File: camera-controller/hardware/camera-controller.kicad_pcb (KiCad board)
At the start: 4 copper layers, 76 parts, among them J1 USB_C_Receptacle_USB2.0_14P, J2 Conn_Coaxial, J3 Conn_01x04, J4 Conn_01x08, J5 Micro_SD_Card_Det1, J6 Conn_01x02, U1 STM32H523RCTx, U2 LR2021, U3 MIC5504-3.3YM5, Y1 32.768MHz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

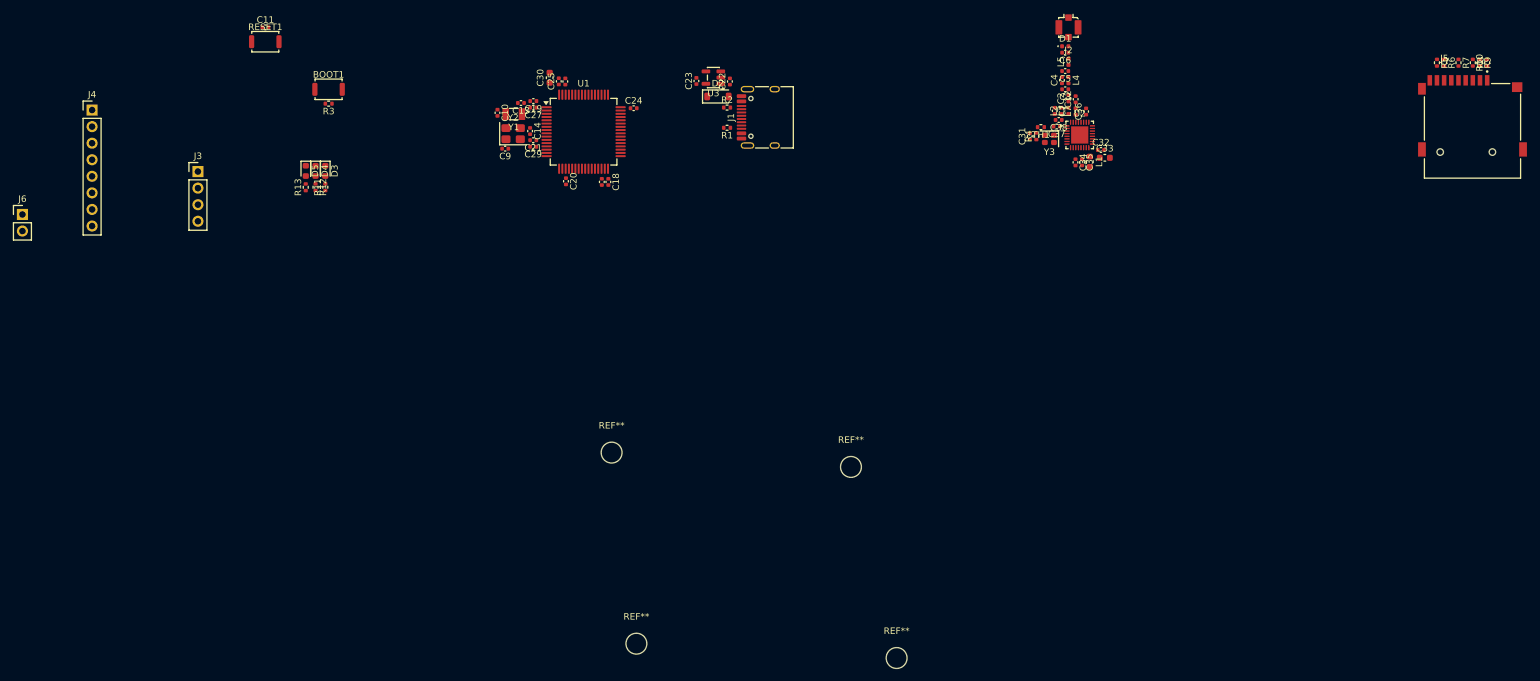
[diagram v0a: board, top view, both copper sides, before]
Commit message: made camera controller pcb layout
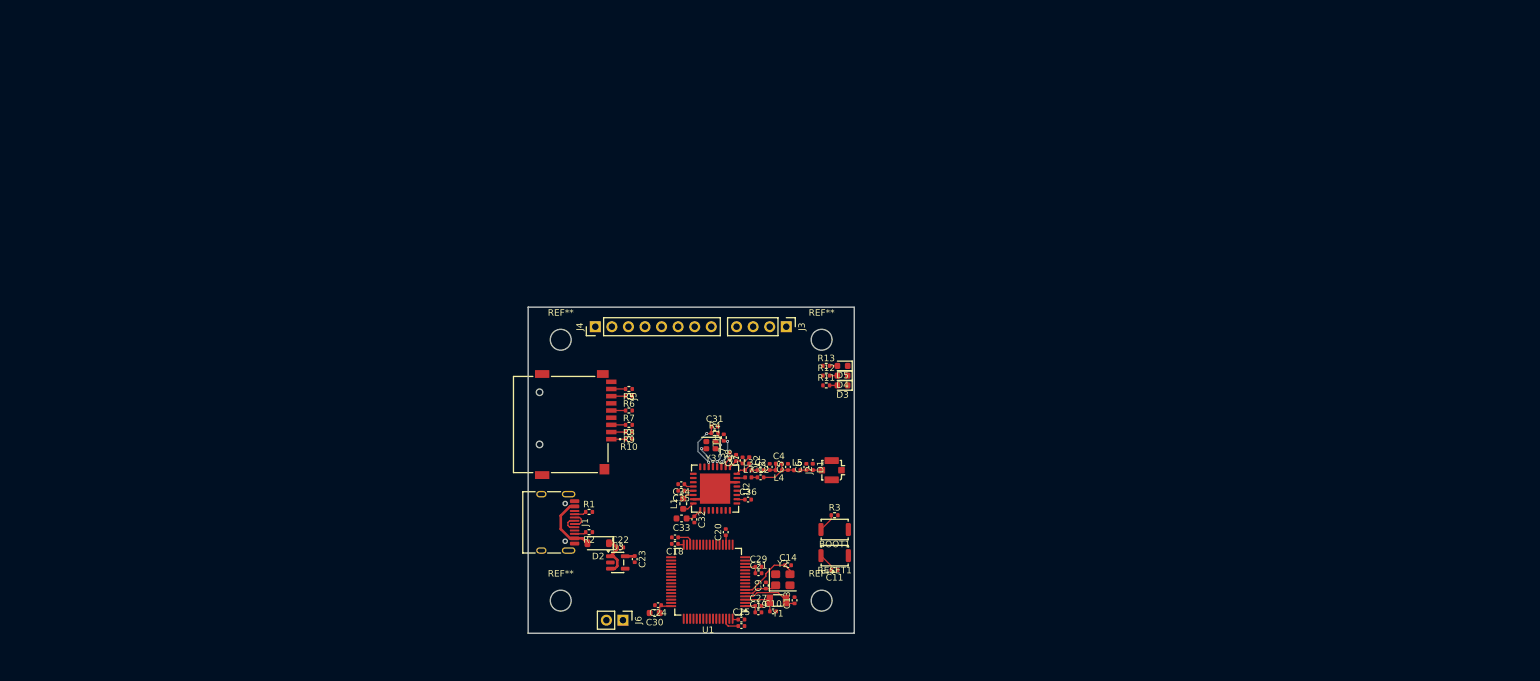
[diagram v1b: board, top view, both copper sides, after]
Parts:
- U2: footprint Package_DFN_QFN:QFN-32-1EP_4x4mm_P0.4mm_EP2.65x2.65mm -> Package_DFN_QFN:QFN-32-1EP_7x7mm_P0.65mm_EP4.65x4.65mm
- moved J5 146.9 mm to (110.0, 83.0), turned to -90 degrees
- moved R10 143.7 mm to (120.5, 85.2), turned to 180 degrees
- moved R9 142.3 mm to (120.5, 84.2), turned to 180 degrees
- moved R8 140.8 mm to (120.5, 83.0), turned to 180 degrees
- moved R7 137.9 mm to (120.5, 80.8), turned to 180 degrees
- moved R6 135.1 mm to (120.5, 78.7), turned to 180 degrees
- moved R5 133.6 mm to (120.5, 77.5), turned to 180 degrees
- moved C11 120.6 mm to (152.0, 105.3), turned to 180 degrees
- moved RESET1 117.6 mm to (152.0, 103.1), turned to 180 degrees
- moved J6 111.1 mm to (119.5, 113.0), turned to -90 degrees
- moved BOOT1 102.8 mm to (152.0, 99.1), turned to 180 degrees
- moved R3 100.0 mm to (152.0, 96.9), turned to 0 degrees
- moved J3 93.3 mm to (144.6, 68.0), turned to -90 degrees
- moved C26 87.8 mm to (137.7, 113.9), turned to 0 degrees
- moved D5 87.6 mm to (153.2, 74.0), turned to 180 degrees
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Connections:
- C7 pad 1: /VRPA -> /VR_PA
- L2 pad 1: /VRPA -> /VR_PA
- U1 pad 14: unconnected-(U1-PA0-Pad14) -> /CAM_STAT
- U1 pad 15: /CAM_STAT -> /LR_STAT
- U1 pad 16: /LR_STAT -> /LR_BUSY
- U1 pad 17: unconnected-(U1-PA3-Pad17) -> /LR_CS
- U1 pad 24: /LR_CS -> /LR_RST
- U1 pad 26: /LR_RST -> /LR_D5
- U1 pad 27: /LR_BUSY -> /LR_D6
- U1 pad 39: /LR_D6 -> unconnected-(U1-PC8-Pad39)
- U1 pad 41: /LR_D5 -> unconnected-(U1-PA8-Pad41)
- U1 pad 42: unconnected-(U1-PA9-Pad42) -> /UART_RX
- U1 pad 43: unconnected-(U1-PA10-Pad43) -> /UART_TX
- U1 pad 49: /SWCKL -> /SWCLK
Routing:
- net +3.3V: track 0.00 -> 15.4 mm
- net Net-(D2-A): track 0.00 -> 9.75 mm
- net /HSE_OUT: track 0.00 -> 9.59 mm
- net /LSE_OUT: track 0.00 -> 8.50 mm
- net /VNTC: track 0.00 -> 8.08 mm, vias 0 -> 2
- net GND: track 0.00 -> 7.75 mm
- net Net-(D2-K): track 0.00 -> 6.75 mm
- net /NTC: track 0.00 -> 6.48 mm, vias 0 -> 2
- net Net-(C12-Pad2): track 0.00 -> 6.13 mm
- net /LSE_IN: track 0.00 -> 5.51 mm
- net /HSE_IN: track 0.00 -> 5.17 mm
- net Net-(U2-XTA): track 0.00 -> 4.52 mm, vias 0 -> 2
- net Net-(U2-XTB): track 0.00 -> 4.28 mm, vias 0 -> 2
- net /VR_PA: track 0.00 -> 3.90 mm
- net Net-(D1-A2): track 0.00 -> 3.32 mm
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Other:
- board outline added: 50 x 50 mm

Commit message: first draft of transceiver pcb
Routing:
- net /VNTC: track 8.08 -> 9.03 mm
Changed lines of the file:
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@@
+	)
+	(segment
+		(start 137.8825 88.98)
+		(end 137.915 88.98)
+		(width 0.2)
+		(layer "F.Cu")
+		(net "/VR_PA")
+	)
+	(segment
+		(start 135.9375 89.4875)
+		(end 135.985 89.4875)
+		(width 0.2)
+		(layer "F.Cu")
+		(net "/VR_PA")
+	)
+	(segment
+		(start 136.8825 88.59)
+		(end 137.4925 88.59)
+		(width 0.2)
+		(layer "F.Cu")
+		(net "/VR_PA")
+	)
+	(segment
+		(start 135.985 89.4875)
+		(end 136.8825 88.59)
+		(width 0.2)
+		(layer "F.Cu")
+		(net "/VR_PA")
+	)
+	(segment
+		(start 137.915 88.98)
+		(end 138.9 87.995)
+		(width 0.2)
+		(layer "F.Cu")
+		(net "/VR_PA")
+	)
+	(segment
+		(start 137.4925 88.59)
+		(end 137.8825 88.98)
+		(width 0.2)
+		(layer "F.Cu")
+		(net "/VR_PA")
 	)
 	(segment
@@
 		(layer "F.Cu")
 		(net "/VDCD")
-	)
-	(segment
-		(start 137.8825 88.98)
-		(end 137.915 88.98)
-		(width 0.2)
-		(layer "F.Cu")
-		(net "/VR_PA")
-	)
-	(segment
-		(start 135.9375 89.4875)
-		(end 135.985 89.4875)
-		(width 0.2)
-		(layer "F.Cu")
-		(net "/VR_PA")
-	)
-	(segment
-		(start 136.8825 88.59)
-		(end 137.4925 88.59)
-		(width 0.2)
-		(layer "F.Cu")
-		(net "/VR_PA")
-	)
-	(segment
-		(start 135.985 89.4875)
-		(end 136.8825 88.59)
-		(width 0.2)
-		(layer "F.Cu")
-		(net "/VR_PA")
-	)
-	(segment
-		(start 137.915 88.98)
-		(end 138.9 87.995)
-		(width 0.2)
-		(layer "F.Cu")
-		(net "/VR_PA")
-	)
-	(segment
-		(start 137.4925 88.59)
-		(end 137.8825 88.98)
-		(width 0.2)
-		(layer "F.Cu")
-		(net "/VR_PA")
 	)
 	(segment
@@
 	)
 	(segment
+		(start 132.795 83.305)
+		(end 132.5 83.6)
+		(width 0.2)
+		(layer "F.Cu")
+		(net "/VNTC")
+	)
+	(segment
 		(start 133.0125 84.385)
 		(end 133.0925 84.305)
@@
 	)
 	(segment
+		(start 133.0925 84.305)
+		(end 133.0925 83.335)
+		(width 0.2)
+		(layer "F.Cu")
+		(net "/VNTC")
+	)
+	(segment
 		(start 133.0925 83.335)
 		(end 133.1225 83.305)
@@
 	)
 	(segment
-		(start 132.3825 84.385)
-		(end 133.0125 84.385)
-		(width 0.2)
-		(layer "F.Cu")
-		(net "/VNTC")
-	)
-	(segment
-		(start 133.0925 84.305)
-		(end 133.0925 83.335)
+		(start 133.1225 83.305)
+		(end 132.795 83.305)
 		(width 0.2)
 		(layer "F.Cu")
@@
 	)
 	(via
-		(at 132.3825 84.385)
+		(at 132.5 83.6)
 		(size 0.45)
 		(drill 0.25)
@@
 	)
 	(segment
-		(start 131.0575 85.71)
-		(end 132.3825 84.385)
+		(start 132.5 83.6)
+		(end 131.0575 85.0425)
 		(width 0.2)
 		(layer "B.Cu")
@@
 	)
 	(segment
+		(start 131.0575 85.0425)
+		(end 131.0575 87.16)
+		(width 0.2)
+		(layer "B.Cu")
+		(net "/VNTC")
+	)
+	(segment
 		(start 131.0575 87.16)
-		(end 131.0575 85.71)
-		(width 0.2)
-		(layer "B.Cu")
-		(net "/VNTC")
-	)
-	(segment
-		(start 132.6825 88.785)
-		(end 131.0575 87.16)
+		(end 132.6825 88.785)
 		(width 0.2)
 		(layer "B.Cu")
@@
 			"1041f301-0349-46e1-8822-e52b4c8b3ef3" "12806317-d077-4186-afc8-4ff6c8b48ca6"
 			"1358a051-eabb-4d72-8740-a3e8340d7430" "14c4fe99-effd-4213-b37c-9940db8c8617"
-			"1bc62bba-f5a6-4853-8b79-c390b3c4d4ec" "22a04720-38bb-4a67-ac98-641396f7d127"
-			"22eb65f4-8c5d-4586-a4b8-ceda9d763b47" "232033eb-20f1-45d0-afbe-8b199121b99f"
+			"16ea95fa-2117-4c31-b320-c81fa461d456" "1bc62bba-f5a6-4853-8b79-c390b3c4d4ec"
+			"22a04720-38bb-4a67-ac98-641396f7d127" "22eb65f4-8c5d-4586-a4b8-ceda9d763b47"
 			"25ba02d5-fe6b-491c-a444-6947921c7fa2" "294f298a-5d62-4bb4-92fc-3cd66b71c9f3"
 			"297e477f-3bd5-466f-97cc-183f80c5a877" "29bd2dab-4127-43d0-8c59-eb513871ad1f"
@@
 			"3c567c16-5b1a-4103-81fa-bbbf8e89759e" "3db08dd0-9d63-4ba8-9f47-7a111a2e8c16"
 			"3efdddb5-215b-4429-a065-ae92ea39b3f6" "3f8e9e50-f241-46df-8971-e3739bbed58e"
-			"4a98f093-3556-46d0-ac74-e7f70d9f5ed7" "4ad88457-1c89-4308-9773-7be579d44e77"
-			"4b459bfa-e7bc-4b6c-a935-ecee057ecc3f" "4cab0f25-4cdd-44b1-b5d6-e5e464ac5cf2"
-			"4dde2c58-0db9-4dc6-9f62-d341adf25ec6" "5093e0a3-720a-424e-a623-362573196668"
-			"53934e35-9437-4c15-ae4b-0d2993678153" "53a3d976-f4e8-4ba2-bc08-6eafea4ac1b6"
-			"53a878ac-959b-45c6-b73e-98e1f2b09d01" "5407e300-0a74-4397-8c8b-c6f9cd2c627a"
-			"54b8e979-e094-4e20-8895-67b28e4b60d9" "55071383-3d0b-42b2-b6ea-09fe577c875e"
-			"568bfd12-2cd2-43ba-837a-8520e3d8815b" "5e81f525-636d-46cd-bfc2-b39449f61016"
+			"41a4a1db-37e9-47e3-bd20-668b57c9d571" "4a98f093-3556-46d0-ac74-e7f70d9f5ed7"
+			"4ad88457-1c89-4308-9773-7be579d44e77" "4b459bfa-e7bc-4b6c-a935-ecee057ecc3f"
+			"4cab0f25-4cdd-44b1-b5d6-e5e464ac5cf2" "4dde2c58-0db9-4dc6-9f62-d341adf25ec6"
+			"5093e0a3-720a-424e-a623-362573196668" "53934e35-9437-4c15-ae4b-0d2993678153"
+			"53a3d976-f4e8-4ba2-bc08-6eafea4ac1b6" "53a878ac-959b-45c6-b73e-98e1f2b09d01"
+			"5407e300-0a74-4397-8c8b-c6f9cd2c627a" "54b8e979-e094-4e20-8895-67b28e4b60d9"
+			"55071383-3d0b-42b2-b6ea-09fe577c875e" "568bfd12-2cd2-43ba-837a-8520e3d8815b"
 			"5f2cc1a4-7456-4aed-8d9e-5917b5e84710" "6182e8bb-4aff-437f-a52e-73305ee6edba"
-			"635f17a9-e630-4d9d-8210-70e7b36fff07" "63c20438-46f6-4ee7-911a-c58d40576bf5"
+			"62fc68d4-692f-437d-9fc9-3114675058b1" "635f17a9-e630-4d9d-8210-70e7b36fff07"
 			"649eaf3d-14d1-4637-bd7a-8235cbd74dd0" "67316d8f-cc4c-4789-b70e-fcd437be1d97"
 			"695e444d-a78e-4130-94c7-af668493d3ea" "6ac16a02-b0d6-4459-bc49-bbcd1f473ad5"
 			"6f00eed7-eb88-4b59-862a-3584900a57c5" "720c3742-8d0d-4a1a-84fd-ceab40c7a67b"
-			"72d330eb-cf0a-423a-af3e-0f59053a2d27" "75741f89-70f7-48fc-9717-0e1a88b932ea"
-			"7674c199-ece3-4afe-8abe-5e29dfa1b6c8" "76a4131d-5475-43ff-8108-0c747d10cfba"
-			"7e145a3e-3f4d-41e9-b5c6-59e226b69e31" "849efa61-3214-4e4a-af83-0731b5feaaf1"
-			"85945e1c-906f-4803-88b2-e16dfa261972" "8a0f1625-f3a6-419f-a61d-bdda690c43e8"
-			"8d874a64-ccb8-438f-92f7-6ada4d00b5d6" "8f86705f-1f0d-4cf8-8f86-7cc5bea4383c"
-			"90ef851c-f283-4d14-ae3a-faacd81f9eaa" "90f95589-5d6c-458d-b048-59728280ffc3"
-			"91911e61-ecf4-4a3a-a55f-f5137acb9df1" "93b8f4ad-d73d-465a-afc3-d70fe772508d"
-			"9411ef35-6e01-47a7-9445-889dcfd4d362" "9533d95d-7d10-45de-aab2-1e666e29bfc4"
-			"96cbc3c5-6301-40fe-afed-c61fb076f1e6" "97cdcbf2-7e5a-4959-944d-bb05dcb87c5a"
-			"9b83c45e-93b8-4577-bb80-e9d2b3b52471" "9b9628f7-a1d7-499f-a8f7-0582cfc36f20"
-			"a7f143a2-e1f0-4685-b604-fcbac470debd" "aff4eafe-7124-464e-a98c-1847028352bc"
-			"b1bdddd2-c456-4039-90d6-b6281ad746cb" "b2a97659-9143-472e-a058-dcf9368037fd"
+			"72d330eb-cf0a-423a-af3e-0f59053a2d27" "7674c199-ece3-4afe-8abe-5e29dfa1b6c8"
+			"76a4131d-5475-43ff-8108-0c747d10cfba" "7e145a3e-3f4d-41e9-b5c6-59e226b69e31"
+			"849efa61-3214-4e4a-af83-0731b5feaaf1" "85945e1c-906f-4803-88b2-e16dfa261972"
+			"8a0f1625-f3a6-419f-a61d-bdda690c43e8" "8d874a64-ccb8-438f-92f7-6ada4d00b5d6"
+			"8f86705f-1f0d-4cf8-8f86-7cc5bea4383c" "90ef851c-f283-4d14-ae3a-faacd81f9eaa"
+			"90f95589-5d6c-458d-b048-59728280ffc3" "91911e61-ecf4-4a3a-a55f-f5137acb9df1"
+			"93b8f4ad-d73d-465a-afc3-d70fe772508d" "9411ef35-6e01-47a7-9445-889dcfd4d362"
+			"9533d95d-7d10-45de-aab2-1e666e29bfc4" "96cbc3c5-6301-40fe-afed-c61fb076f1e6"
+			"97cdcbf2-7e5a-4959-944d-bb05dcb87c5a" "9b83c45e-93b8-4577-bb80-e9d2b3b52471"
+			"9b9628f7-a1d7-499f-a8f7-0582cfc36f20" "a7f143a2-e1f0-4685-b604-fcbac470debd"
+			"a94a33b1-ec3a-4786-810a-3eeae708a369" "abc65c81-b8fd-445e-ac8e-9e2747afd620"
+			"aff4eafe-7124-464e-a98c-1847028352bc" "b1bdddd2-c456-4039-90d6-b6281ad746cb"
 			"b835949e-edba-4653-8c6a-576bc1b88d6c" "bb30fddc-0220-4993-a194-7e83466d521d"
 			"bcd33461-d973-4b4d-b735-e3e06b90e1d1" "bdb85e52-b1be-45e6-bb12-bc199d1fdd7f"
@@
 			"c5f2284a-7ea0-4470-9b35-ee9dadfd42aa" "c80ebf6f-8e0a-4934-ac7b-74e1ed840b3d"
 			"c8410ad5-1991-4611-bc05-fd26bc2dbf81" "ca0ad787-952d-4f69-9e1e-b1de511cfd63"
-			"cd62c01a-79e3-4cc3-8e91-04355e55cb51" "ce8f2ddd-a142-48f1-8302-e4928810bbbb"
-			"d059787a-41eb-4459-9b92-2bc2f974cbd5" "d2724d46-31c9-461b-b6f8-bc8ed4a375e8"
-			"d3db9992-162a-413c-add7-707a124ae330" "d689d873-4c1c-4f05-821c-25bfc899cac7"
-			"d7723886-3e24-4ac6-b601-714c50871033" "da51e7eb-8af1-46fc-a686-1555ca50d49c"
-			"de00b40c-f0a4-4855-99b1-0134baa2c68a" "ea8869f9-0015-4535-a6bd-c59bbf5a7232"
+			"ce8f2ddd-a142-48f1-8302-e4928810bbbb" "d059787a-41eb-4459-9b92-2bc2f974cbd5"
+			"d2724d46-31c9-461b-b6f8-bc8ed4a375e8" "d3db9992-162a-413c-add7-707a124ae330"
+			"d689d873-4c1c-4f05-821c-25bfc899cac7" "d7723886-3e24-4ac6-b601-714c50871033"
+			"da51e7eb-8af1-46fc-a686-1555ca50d49c" "de00b40c-f0a4-4855-99b1-0134baa2c68a"
+			"dfdfefcf-16e8-44b0-a5d3-4760554c8ce5" "ea8869f9-0015-4535-a6bd-c59bbf5a7232"
 			"ebbd6a3b-182f-47ea-be82-10a87831473f" "ec00e219-6db6-48f9-8c29-6f43fb25f26b"
-			"ec80b570-f99b-4a77-9512-1e8a8d8c6b10" "ee09e8fc-de5e-4cd6-b59c-862bca51a696"
-			"f111fdb8-8d0c-43ce-a812-f9c0d61d8081" "f3fe035a-4c7c-4c7c-b576-b7ed83b3ddcb"
-			"f66bdb33-c91a-4fce-9f2d-7c63be4f6b6f" "f72c7c3a-47da-48b5-adee-efe35439dea7"
-			"f8804ffa-7350-49da-be8d-2334f7638e7e" "f93c4614-8cdd-4a7b-8ce0-35ce11aafb43"
-			"fdcd65bc-2984-43d5-86df-5367c3f8b5ab" "feaef577-9b75-4cfd-a564-bb67bc0ca13f"
+			"ec5d37f8-32bd-43e4-adc1-4cde7720c741" "ec80b570-f99b-4a77-9512-1e8a8d8c6b10"
+			"ee09e8fc-de5e-4cd6-b59c-862bca51a696" "f111fdb8-8d0c-43ce-a812-f9c0d61d8081"
+			"f3fe035a-4c7c-4c7c-b576-b7ed83b3ddcb" "f66bdb33-c91a-4fce-9f2d-7c63be4f6b6f"
+			"f72c7c3a-47da-48b5-adee-efe35439dea7" "f8804ffa-7350-49da-be8d-2334f7638e7e"
+			"f93c4614-8cdd-4a7b-8ce0-35ce11aafb43" "fdcd65bc-2984-43d5-86df-5367c3f8b5ab"
+			"feaef577-9b75-4cfd-a564-bb67bc0ca13f"
 		)
 	)

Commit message: updated board and started frame
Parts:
- moved C22 54.9 mm to (81.0, 62.2)
- moved R1 54.9 mm to (76.3, 56.8)
- moved U3 54.9 mm to (80.7, 64.5)
- moved D2 54.9 mm to (77.7, 61.6)
- moved J1 54.9 mm to (70.0, 58.4)
- moved R2 54.9 mm to (76.3, 59.9)
- moved C23 54.9 mm to (83.3, 64.0)
- moved J3 41.9 mm to (132.2, 108.0), turned to 90 degrees
- moved R3 37.7 mm to (119.3, 78.2), turned to 90 degrees
- moved BOOT1 37.0 mm to (121.5, 78.2), turned to -90 degrees
- moved C11 36.4 mm to (127.7, 78.2), turned to -90 degrees
- moved RESET1 36.4 mm to (125.5, 78.2), turned to -90 degrees
- moved C10 24.7 mm to (146.1, 87.2)
- moved C13 24.7 mm to (149.3, 85.5)
- moved C14 24.7 mm to (148.3, 80.1)
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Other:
- board size 50 x 50 mm -> 40 x 40 mm

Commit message: finished camera controller pcb
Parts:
- removed C22, C23: 1uF, Capacitor_SMD:C_0402_1005Metric
- removed D2: D_Schottky, Diode_SMD:D_SOD-123
- removed J1: USB_C_Receptacle_USB2.0_14P, Connector_USB:USB_C_Receptacle_HRO_TYPE-C-31-M-12
- removed R1, R2: 5.1K, Resistor_SMD:R_0402_1005Metric
- removed U3: MIC5504-3.3YM5, Package_TO_SOT_SMD:SOT-23-5
- moved C19 1.00 mm to (143.7, 88.3)
- moved C27 1.00 mm to (143.7, 87.3)
- moved C30 0.90 mm to (129.4, 88.6)
- moved L1 0.53 mm to (124.2, 103.6)
- moved R10 0.45 mm to (124.8, 92.7)
- moved R5 0.45 mm to (124.8, 85.0)
- moved R6 0.45 mm to (124.8, 86.0)
- moved R7 0.45 mm to (124.8, 88.2)
- moved R8 0.45 mm to (124.8, 90.5)
- moved R9 0.45 mm to (124.8, 91.5)
- moved C13 0.45 mm to (148.9, 85.5)
- moved C10 0.40 mm to (145.7, 87.2)
- moved Y1 0.40 mm to (146.4, 85.5)
- moved C20 0.10 mm to (138.8, 74.9)
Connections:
- C34 pad 1: /VDCD -> /VDCC1
- C35 pad 1: /VPAX -> /VPAX1
- C36 pad 1: /VDCD -> /VDCC2
- C37 pad 1: /VPAX -> /VPAX2
- U2 pad 12: /VDCD -> /VDCC1
- U2 pad 13: /VPAX -> /VPAX1
- U2 pad 2: /VPAX -> /VPAX2
- U2 pad 26: /VDCD -> /VDCC2
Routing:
- net GND: track 7.75 -> 63.8 mm, vias 0 -> 232
- net /MOSI: track 0.00 -> 45.7 mm, vias 0 -> 2
- net /MISO: track 0.00 -> 44.7 mm, vias 0 -> 2
- net /SCK: track 0.00 -> 41.9 mm, vias 0 -> 2
- net /LR_D5: track 0.00 -> 34.6 mm, vias 0 -> 2
- net /LR_CS: track 0.00 -> 33.1 mm, vias 0 -> 2
- net /LR_RST: track 0.00 -> 32.6 mm, vias 0 -> 2
- net /LR_D6: track 0.00 -> 32.4 mm, vias 0 -> 2
- net /LR_BUSY: track 0.00 -> 30.8 mm, vias 0 -> 2
- net +3.3V: track 15.1 -> 44.6 mm, vias 0 -> 12
- net /UART_TX: track 0.00 -> 29.0 mm, vias 0 -> 1
- net /SWDIO: track 0.00 -> 28.9 mm, vias 0 -> 1
- net /UART_RX: track 0.00 -> 28.1 mm, vias 0 -> 1
- net /SCL: track 0.00 -> 26.8 mm, vias 0 -> 1
- net /LR_D11: track 0.00 -> 24.4 mm, vias 0 -> 2
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- added copper zone on In1.Cu, net +3.3V
- added copper zone on B.Cu, net GND
- added copper zone on F.Cu, net GND
- added copper zone on In2.Cu, net GND
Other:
- board text added: "+"
- board text added: "BOOT"
- board text added: "RST"
- board text added: "SWCLK"
- board text added: "SWIO"
